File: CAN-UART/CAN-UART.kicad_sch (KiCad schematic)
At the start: 14 parts, among them P1 USB_C_Plug_USB2.0, U1 AP2112K-3.3, U2 SN65HVD230, U3 ESP32-C3

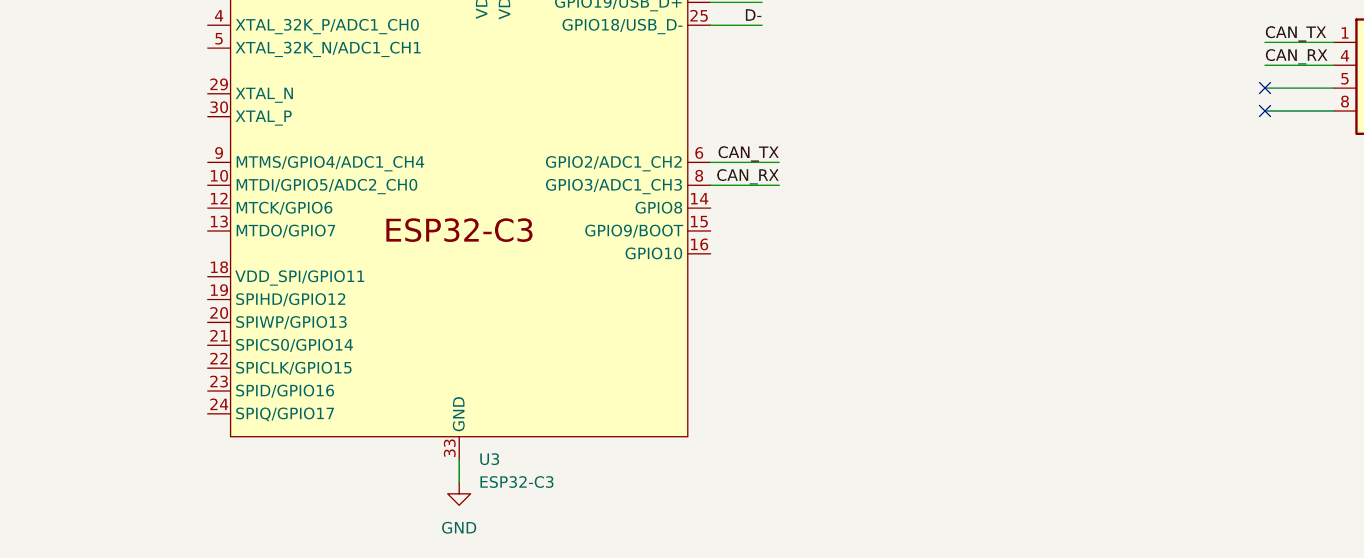
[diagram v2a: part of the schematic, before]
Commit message: Added 16MB flash for esp32
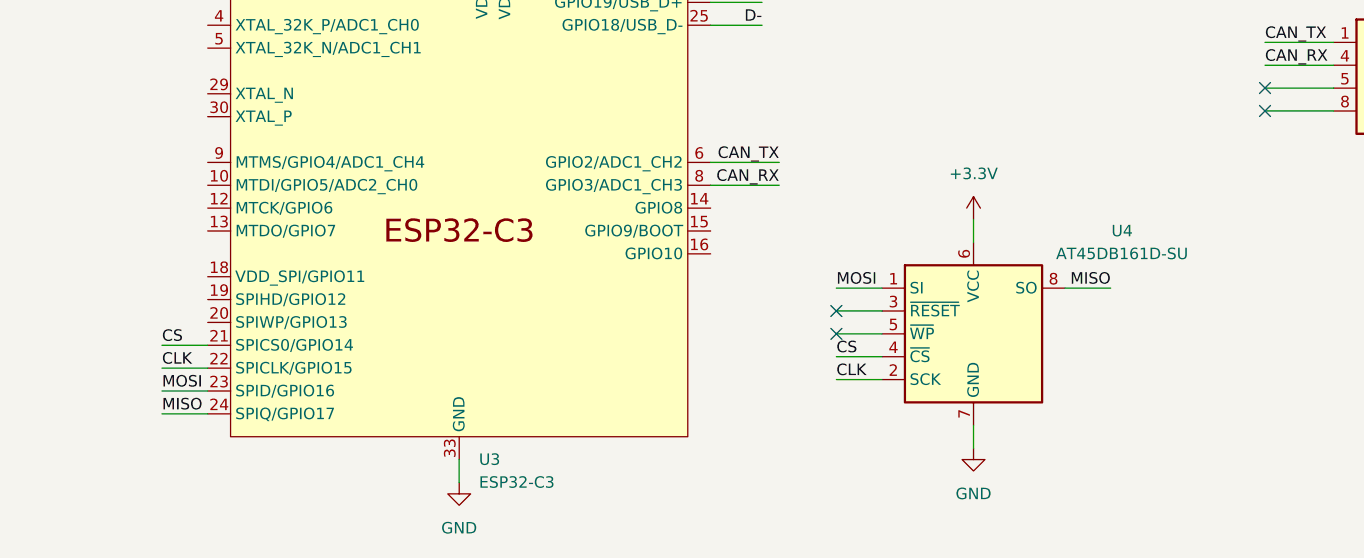
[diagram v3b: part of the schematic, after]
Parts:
- added U4: AT45DB161D-SU, Package_SO:SOIC-8_5.275x5.275mm_P1.27mm, symbol Memory_Flash:AT45DB161D-SU
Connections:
- net +3.3V: now also U4.6 (VCC)
- net GND: now also U4.7 (GND)
- net CS: now reaches U3.21 (SPICS0/GPIO14)
- net CS: now also U4.4 (~{CS})
- net CLK: now reaches U3.22 (SPICLK/GPIO15)
- net CLK: now also U4.2 (SCK)
- net MOSI: now reaches U3.23 (SPID/GPIO16)
- net MOSI: now also U4.1 (SI)
- net MISO: now reaches U3.24 (SPIQ/GPIO17)
- net MISO: now also U4.8 (SO)
- no-connect marks 3 -> 5
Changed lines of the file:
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@@
   (no_connect (at 210.185 123.825))
   (no_connect (at 57.15 39.37))
+  (no_connect (at 162.56 146.05))
   (no_connect (at 210.185 121.285))
+  (no_connect (at 162.56 148.59))
   (wire (pts (xy 139.7 24.13) (xy 139.7 30.48))
     (stroke (width 0) (type default))
@@
     (stroke (width 0) (type default))
   )
+  (wire (pts (xy 162.56 153.67) (xy 167.64 153.67))
+    (stroke (width 0) (type default))
+  )
   (wire (pts (xy 29.21 72.39) (xy 36.83 72.39))
     (stroke (width 0) (type default))
@@
     (stroke (width 0) (type default))
   )
+  (wire (pts (xy 162.56 146.05) (xy 167.64 146.05))
+    (stroke (width 0) (type default))
+  )
   (wire (pts (xy 52.07 36.83) (xy 57.15 36.83))
     (stroke (width 0) (type default))
   )
+  (wire (pts (xy 87.63 152.4) (xy 92.71 152.4))
+    (stroke (width 0) (type default))
+  )
   (wire (pts (xy 57.15 49.53) (xy 52.07 49.53))
     (stroke (width 0) (type default))
@@
     (stroke (width 0) (type default))
   )
+  (wire (pts (xy 87.63 149.86) (xy 92.71 149.86))
+    (stroke (width 0) (type default))
+  )
   (wire (pts (xy 67.31 36.83) (xy 64.77 36.83))
     (stroke (width 0) (type default))
@@
     (stroke (width 0) (type default))
   )
+  (wire (pts (xy 187.96 143.51) (xy 193.04 143.51))
+    (stroke (width 0) (type default))
+  )
+  (wire (pts (xy 177.8 158.75) (xy 177.8 161.29))
+    (stroke (width 0) (type default))
+  )
   (wire (pts (xy 148.59 111.76) (xy 154.305 111.76))
     (stroke (width 0) (type default))
@@
     (stroke (width 0) (type default))
   )
+  (wire (pts (xy 177.8 135.89) (xy 177.8 138.43))
+    (stroke (width 0) (type default))
+  )
   (wire (pts (xy 81.28 33.02) (xy 86.36 33.02))
     (stroke (width 0) (type default))
@@
     (stroke (width 0) (type default))
   )
+  (wire (pts (xy 162.56 148.59) (xy 167.64 148.59))
+    (stroke (width 0) (type default))
+  )
   (wire (pts (xy 125.73 96.52) (xy 125.73 99.06))
     (stroke (width 0) (type default))
@@
     (stroke (width 0) (type default))
   )
+  (wire (pts (xy 87.63 154.94) (xy 92.71 154.94))
+    (stroke (width 0) (type default))
+  )
   (wire (pts (xy 121.92 96.52) (xy 123.19 96.52))
     (stroke (width 0) (type default))
@@
     (stroke (width 0) (type default))
   )
+  (wire (pts (xy 162.56 151.13) (xy 167.64 151.13))
+    (stroke (width 0) (type default))
+  )
   (wire (pts (xy 148.59 106.68) (xy 154.305 106.68))
     (stroke (width 0) (type default))
@@
     (stroke (width 0) (type default))
   )
+  (wire (pts (xy 162.56 143.51) (xy 167.64 143.51))
+    (stroke (width 0) (type default))
+  )
   (wire (pts (xy 121.92 93.98) (xy 121.92 96.52))
+    (stroke (width 0) (type default))
+  )
+  (wire (pts (xy 92.71 157.48) (xy 87.63 157.48))
     (stroke (width 0) (type default))
   )
@@
     (effects (font (size 2.54 2.54)) (justify left bottom))
   )
+  (label "MOSI" (at 162.56 143.51 0) (fields_autoplaced)
+    (effects (font (size 1.27 1.27)) (justify left bottom))
+  )
+  (label "CS" (at 162.56 151.13 0) (fields_autoplaced)
+    (effects (font (size 1.27 1.27)) (justify left bottom))
+  )
   (label "D-" (at 154.305 114.3 180) (fields_autoplaced)
     (effects (font (size 1.27 1.27)) (justify right bottom))
   )
+  (label "MISO" (at 193.04 143.51 180) (fields_autoplaced)
+    (effects (font (size 1.27 1.27)) (justify right bottom))
+  )
   (label "CAN_RX" (at 210.185 118.745 0) (fields_autoplaced)
     (effects (font (size 1.27 1.27)) (justify left bottom))
@@
     (effects (font (size 1.27 1.27)) (justify right bottom))
   )
+  (label "CLK" (at 162.56 153.67 0) (fields_autoplaced)
+    (effects (font (size 1.27 1.27)) (justify left bottom))
+  )
+  (label "MOSI" (at 87.63 154.94 0) (fields_autoplaced)
+    (effects (font (size 1.27 1.27)) (justify left bottom))
+  )
   (label "CAN_TX" (at 210.185 116.205 0) (fields_autoplaced)
+    (effects (font (size 1.27 1.27)) (justify left bottom))
+  )
+  (label "CLK" (at 87.63 152.4 0) (fields_autoplaced)
+    (effects (font (size 1.27 1.27)) (justify left bottom))
+  )
+  (label "MISO" (at 87.63 157.48 0) (fields_autoplaced)
+    (effects (font (size 1.27 1.27)) (justify left bottom))
+  )
+  (label "CS" (at 87.63 149.86 0) (fields_autoplaced)
     (effects (font (size 1.27 1.27)) (justify left bottom))
   )
@@
     )
   )
-  (symbol (lib_id "Interface_CAN_LIN:SN65HVD230") (at 227.965 118.745 0) (unit 1)
-    (in_bom yes) (on_board yes) (dnp no) (fields_autoplaced)
-    (property "Reference" "U2" (at 229.9209 108.585 0)
-      (effects (font (size 1.27 1.27)) (justify left))
-    )
-    (property "Value" "SN65HVD230" (at 229.9209 111.125 0)
-      (effects (font (size 1.27 1.27)) (justify left))
-    )
-    (property "Footprint" "Package_SO:SOIC-8_3.9x4.9mm_P1.27mm" (at 227.965 131.445 0)
-      (effects (font (size 1.27 1.27)) hide)
-    )
-    (property "Datasheet" "http://www.ti.com/lit/ds/symlink/sn65hvd230.pdf" (at 225.425 108.585 0)
+  (symbol (lib_id "Memory_Flash:AT45DB161D-SU") (at 177.8 148.59 0) (unit 1)
+    (in_bom yes) (on_board yes) (dnp no)
+    (property "Reference" "U4" (at 194.31 137.16 0)
+      (effects (font (size 1.27 1.27)))
+    )
+    (property "Value" "AT45DB161D-SU" (at 194.31 139.7 0)
+      (effects (font (size 1.27 1.27)))
+    )
+    (property "Footprint" "Package_SO:SOIC-8_5.275x5.275mm_P1.27mm" (at 207.01 163.83 0)
+      (effects (font (size 1.27 1.27)) hide)
+    )
+    (property "Datasheet" "https://www.adestotech.com/wp-content/uploads/doc3500.pdf" (at 177.8 148.59 0)
       (effects (font (size 1.27 1.27)) hide)
     )
@@
       (project "CAN-UART"
         (path "/21020eba-b649-4135-9bee-384d0a5cab58"
+          (reference "U4") (unit 1)
+        )
+      )
+    )
+  )
+  (symbol (lib_id "Interface_CAN_LIN:SN65HVD230") (at 227.965 118.745 0) (unit 1)
+    (in_bom yes) (on_board yes) (dnp no) (fields_autoplaced)
+    (property "Reference" "U2" (at 229.9209 108.585 0)
+      (effects (font (size 1.27 1.27)) (justify left))
+    )
+    (property "Value" "SN65HVD230" (at 229.9209 111.125 0)
+      (effects (font (size 1.27 1.27)) (justify left))
+    )
+    (property "Footprint" "Package_SO:SOIC-8_3.9x4.9mm_P1.27mm" (at 227.965 131.445 0)
+      (effects (font (size 1.27 1.27)) hide)
+    )
+    (property "Datasheet" "http://www.ti.com/lit/ds/symlink/sn65hvd230.pdf" (at 225.425 108.585 0)
+      (effects (font (size 1.27 1.27)) hide)
+    )
+    (pin "1")
+    (pin "2")
+    (pin "3")
+    (pin "4")
+    (pin "5")
+    (pin "6")
+    (pin "7")
+    (pin "8")
+    (instances
+      (project "CAN-UART"
+        (path "/21020eba-b649-4135-9bee-384d0a5cab58"
           (reference "U2") (unit 1)
+        )
+      )
+    )
+  )
+  (symbol (lib_name "GND_3") (lib_id "power:GND") (at 177.8 161.29 0) (unit 1)
+    (in_bom yes) (on_board yes) (dnp no) (fields_autoplaced)
+    (property "Reference" "#PWR011" (at 177.8 167.64 0)
+      (effects (font (size 1.27 1.27)) hide)
+    )
+    (property "Value" "GND" (at 177.8 166.37 0)
+      (effects (font (size 1.27 1.27)))
+    )
+    (property "Footprint" "" (at 177.8 161.29 0)
+      (effects (font (size 1.27 1.27)) hide)
+    )
+    (property "Datasheet" "" (at 177.8 161.29 0)
+      (effects (font (size 1.27 1.27)) hide)
+    )
+    (pin "1")
+    (instances
+      (project "CAN-UART"
+        (path "/21020eba-b649-4135-9bee-384d0a5cab58"
+          (reference "#PWR011") (unit 1)
         )
       )
@@
         )
       )
+    )
+  )
+  (symbol (lib_id "power:+3.3V") (at 177.8 135.89 0) (unit 1)
+    (in_bom yes) (on_board yes) (dnp no) (fields_autoplaced)
+    (property "Reference" "#PWR012" (at 177.8 139.7 0)
+      (effects (font (size 1.27 1.27)) hide)
+    )
+    (property "Value" "+3.3V" (at 177.8 130.81 0)
+      (effects (font (size 1.27 1.27)))
+    )
+    (property "Footprint" "" (at 177.8 135.89 0)
+      (effects (font (size 1.27 1.27)) hide)
+    )
+    (property "Datasheet" "" (at 177.8 135.89 0)
+      (effects (font (size 1.27 1.27)) hide)
+    )
+    (pin "1")
+    (instances
+      (project "CAN-UART"
+        (path "/21020eba-b649-4135-9bee-384d0a5cab58"
+          (reference "#PWR012") (unit 1)
+        )
+      )

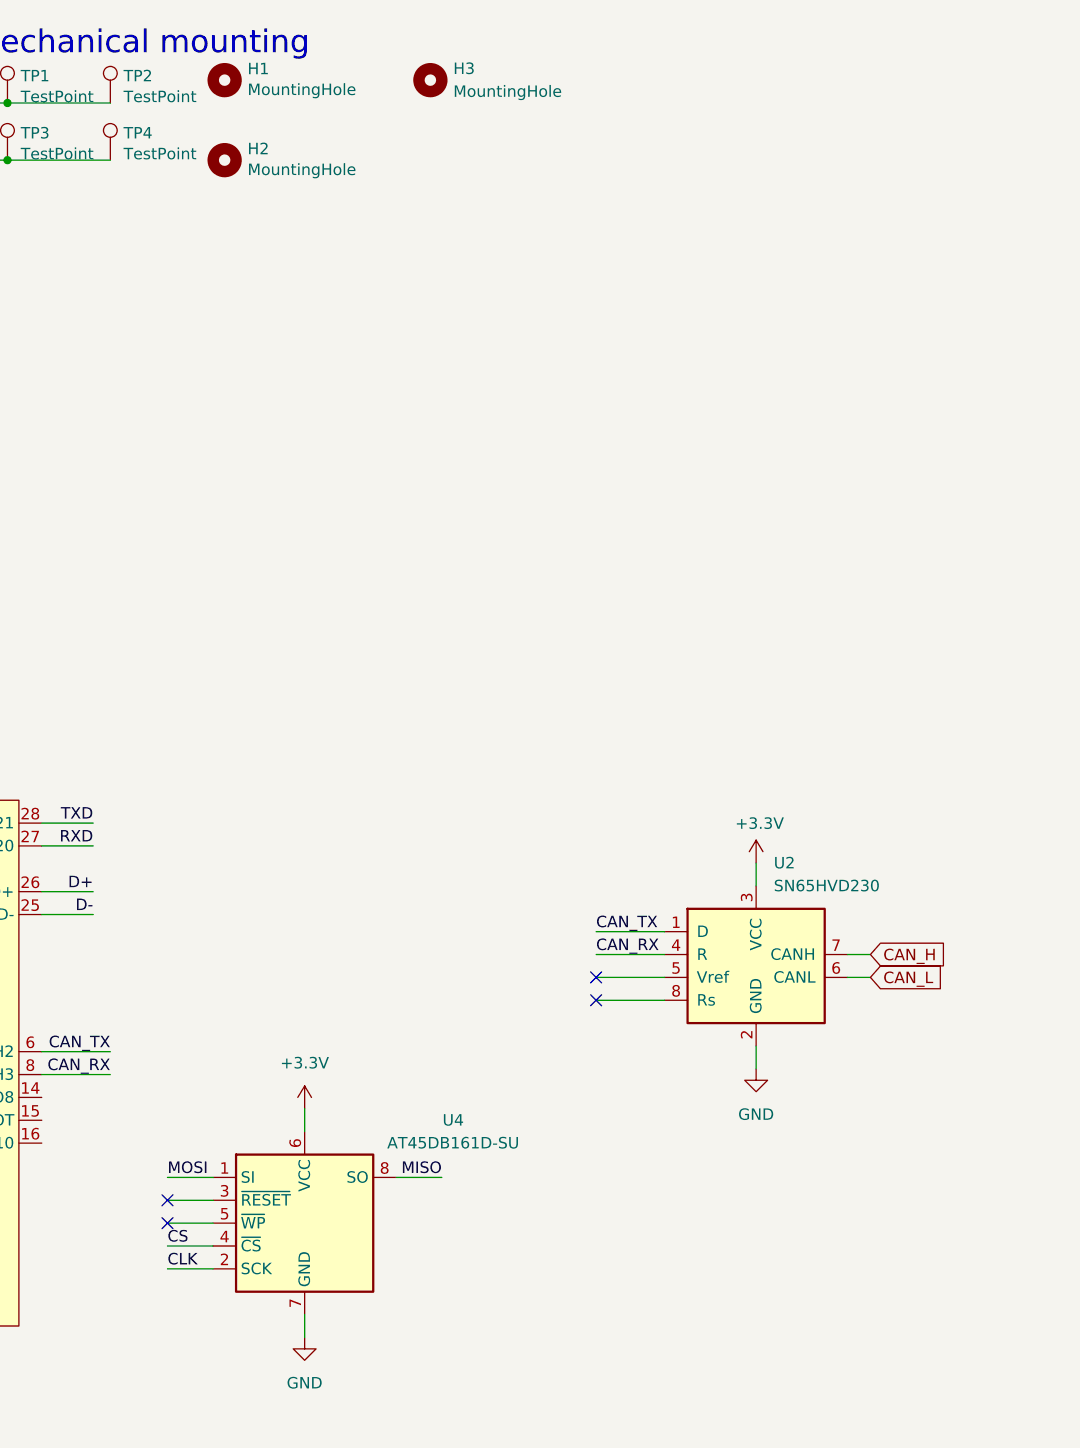
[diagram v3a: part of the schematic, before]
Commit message: Added external connector
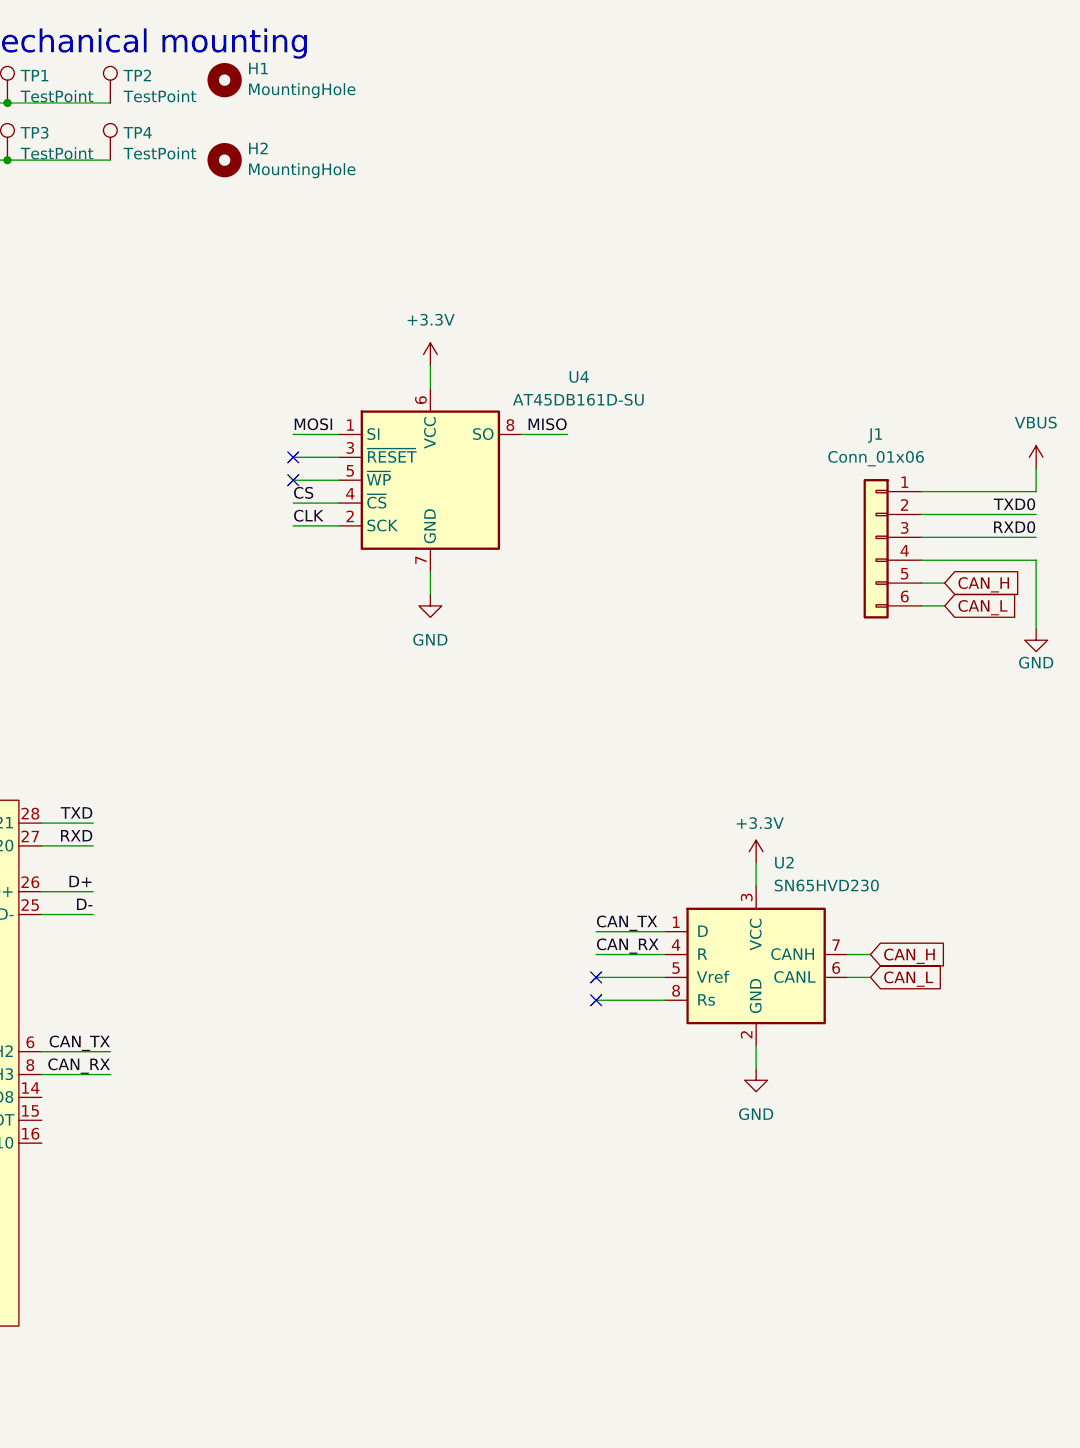
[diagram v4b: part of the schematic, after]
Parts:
- removed H3: MountingHole, MountingHole:MountingHole_2.2mm_M2, symbol Mechanical:MountingHole
- added J1: Conn_01x06, Connector_PinSocket_2.00mm:PinSocket_1x06_P2.00mm_Horizontal, symbol Connector_Generic:Conn_01x06
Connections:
- net CAN_H: now also J1.5 (Pin_5)
- net CAN_L: now also J1.6 (Pin_6)
- net GND: now also J1.4 (Pin_4)
- net VBUS: now also J1.1 (Pin_1)
- new net RXD0: J1.3 (Pin_3)
- new net TXD0: J1.2 (Pin_2)
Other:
- moved on the sheet: U4
